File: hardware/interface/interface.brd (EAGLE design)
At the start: 112 x 83 mm, 8 parts

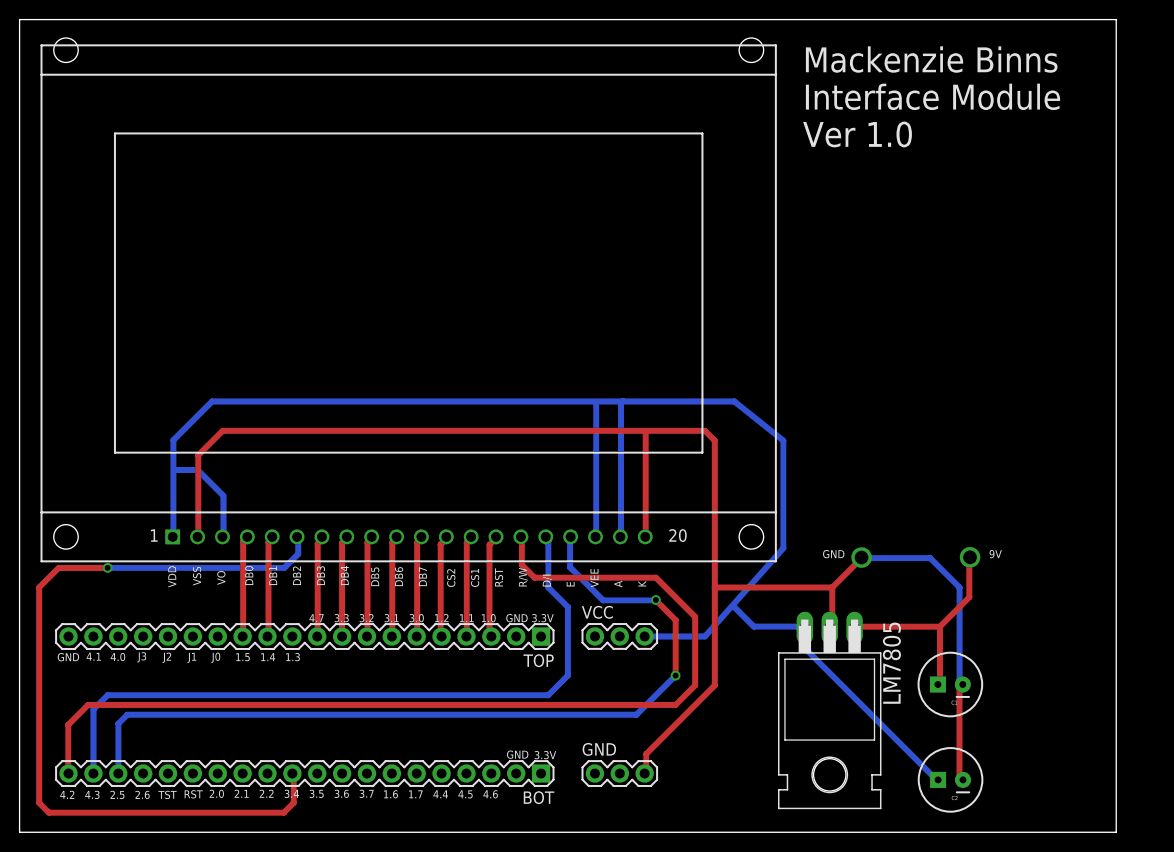
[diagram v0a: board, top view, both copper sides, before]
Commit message: update interface schematic
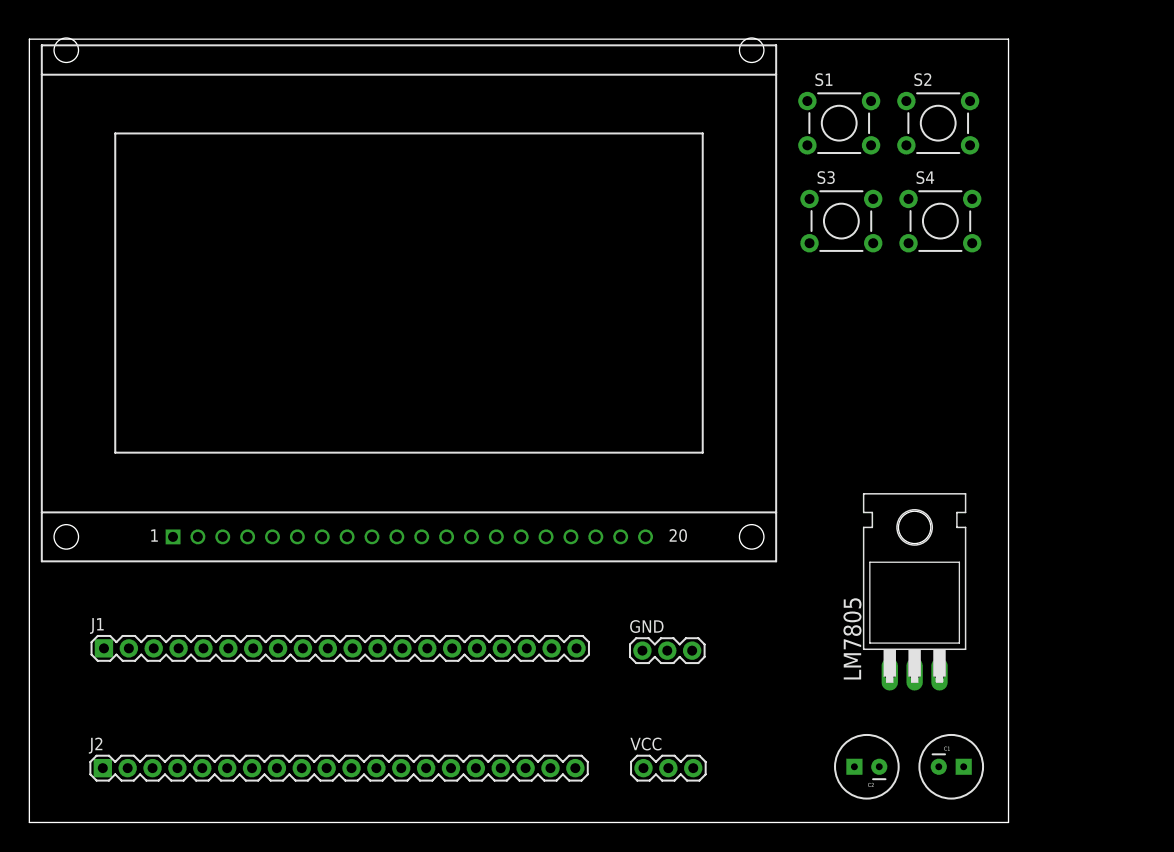
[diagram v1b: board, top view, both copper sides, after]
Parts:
- removed BOT, TOP: (no value), SparkFun-Connectors:1X20
- added J1, J2: (no value), SparkFun-Connectors:1X20
- added S1: Set, SparkFun-Retired:TACTILE-PTH
- added S2: Clear, SparkFun-Retired:TACTILE-PTH
- added S3: Shift Up, SparkFun-Retired:TACTILE-PTH
- added S4: Shift Down, SparkFun-Retired:TACTILE-PTH
- moved LM7805 17.9 mm to (90.4, 25.3), turned to 0 degrees
- moved VCC 14.3 mm to (62.7, 5.55)
- moved GND 13.5 mm to (62.6, 17.6)
- moved C2 8.65 mm to (85.5, 5.69)
- moved C1 8.40 mm to (94.2, 5.69), turned to 0 degrees
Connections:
- new net N$2: S1.1
- new net N$3: S1.3
- new net N$4: S2.1
- new net N$5: S2.3
- new net N$6: S3.1
- new net N$7: S3.3
- new net N$8: S4.1
- new net N$9: S4.3
- net GND: now also GND.1, GND.2, GND.3
- net P1.0: now also J2.18
- net P1.1: now also J2.17
- net P1.2: now also J2.16
- net P1.4: now also J2.9
- net P1.5: now also J2.8
- net P2.5: now also J1.3
- net P3.0: now also J2.15
- net P3.1: now also J2.14
- net P3.2: now also J2.13
- net P3.3: now also J2.12
- net P3.4: now also J1.12
- net P4.2: now also J1.1
- net P4.3: now also J1.2
- net P4.7: now also J2.11
- net VCC: now also VCC.1, VCC.2, VCC.3
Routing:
- net N$29: track 119.7 -> 0.00 mm
- net N$1: track 104.6 -> 0.00 mm
- net N$18: track 99.8 -> 0.00 mm
- net N$9: track 81.4 -> 0.00 mm, vias 1 -> 0
- net N$20: track 72.6 -> 0.00 mm, vias 1 -> 0
- net N$19: track 71.4 -> 0.00 mm
- net N$26: track 29.6 -> 0.00 mm
- net N$27: track 23.2 -> 0.00 mm
- net N$30: track 21.5 -> 0.00 mm
- net N$3: track 14.0 -> 0.00 mm
- net N$4: track 13.9 -> 0.00 mm
- net N$22: track 13.3 -> 0.00 mm
- net N$6: track 10.8 -> 0.00 mm
- net N$17: track 10.5 -> 0.00 mm
- net N$7: track 10.5 -> 0.00 mm
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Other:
- board size 112 x 83 mm -> 100 x 80 mm
- board text added: "Interface Board Derailleurs"
- board text removed: "1.4 1.3"
- board text removed: "1.5"
- board text removed: "1.6 1.7 4.4 4.5 4.6"
- board text removed: "2.0 2.1 2.2 3.4 3.5 3.6 3.7"
- board text removed: "3.3V"
- board text removed: "4.0"
- board text removed: "4.1"
- board text removed: "4.2 4.3 2.5 2.6"
- board text removed: "4.7 3.3 3.2 3.1 3.0 1.2 1.1 1.0 GND 3.3V"
- board text removed: "9V"
- board text removed: "CS2 CS1 RST R/W D/I E VEE A K"
- board text removed: "DB0 DB1 DB2 DB3 DB4"
- board text removed: "DB5 DB6 DB7"
- board text removed: "GND"
- board text removed: "J0"
- board text removed: "J1"
- board text removed: "J2"
- board text removed: "J3"
- board text removed: "Mackenzie Binns Interface Module Ver 1.0"
- board text removed: "RST"
- board text removed: "TST"
- board text removed: "VDD"
- board text removed: "VO"
- board text removed: "VSS"

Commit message: finish boards
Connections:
- removed net N$2: S1.1
- removed net N$3: S1.3
- removed net N$4: S2.1
- removed net N$5: S2.3
- removed net N$6: S3.1
- removed net N$7: S3.3
- removed net N$8: S4.1
- removed net N$9: S4.3
- new net P2.0: J1.7, S1.3
- new net P2.6: J1.4, S2.3
- new net P3.5: J1.11, S3.3
- new net P3.6: J1.12, S4.3
- net GND: now also S1.1, S2.1, S3.1, S4.1
- net P3.4: now also J1.10; no longer J1.12
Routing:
- net GND: track 0.00 -> 179.0 mm
- net VCC: track 0.00 -> 119.6 mm
- net P2.6: track 0.00 -> 98.8 mm
- net P2.0: track 0.00 -> 82.9 mm
- net P4.7: track 0.00 -> 74.6 mm
- net P3.6: track 0.00 -> 74.6 mm
- net P3.5: track 0.00 -> 72.5 mm
- net P3.2: track 0.00 -> 62.7 mm, vias 0 -> 1
- net P3.0: track 0.00 -> 50.8 mm, vias 0 -> 1
- net P4.2: track 0.00 -> 48.9 mm
- net P4.3: track 0.00 -> 47.8 mm
- net P2.5: track 0.00 -> 47.3 mm
- net P3.1: track 0.00 -> 46.8 mm, vias 0 -> 1
- net P1.5: track 0.00 -> 46.2 mm
- net P1.4: track 0.00 -> 40.4 mm, vias 0 -> 1
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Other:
- board text added: "Clear"
- board text added: "Set"
- board text added: "Shift Down"
- board text added: "Shift Up"

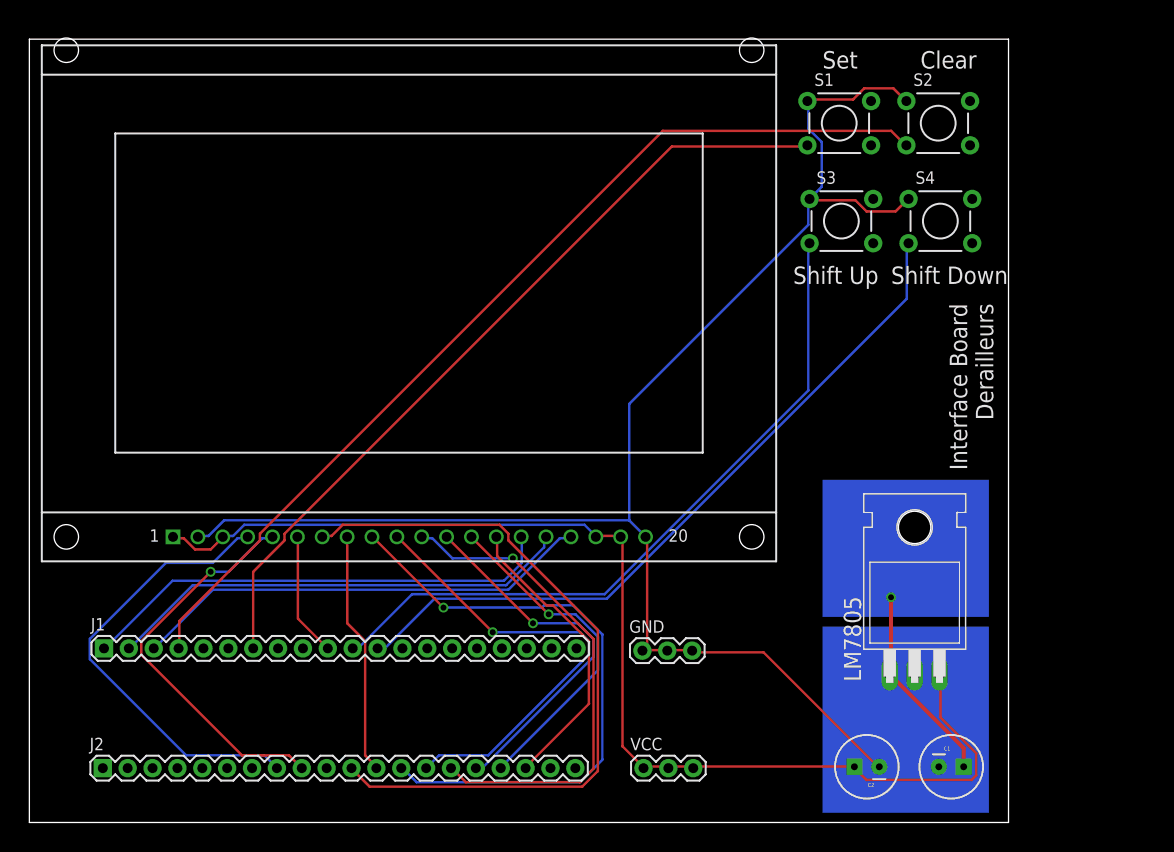
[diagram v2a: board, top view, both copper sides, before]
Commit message: Finish routing all boards, schematics are consitant, and all deliverable requirements are met..
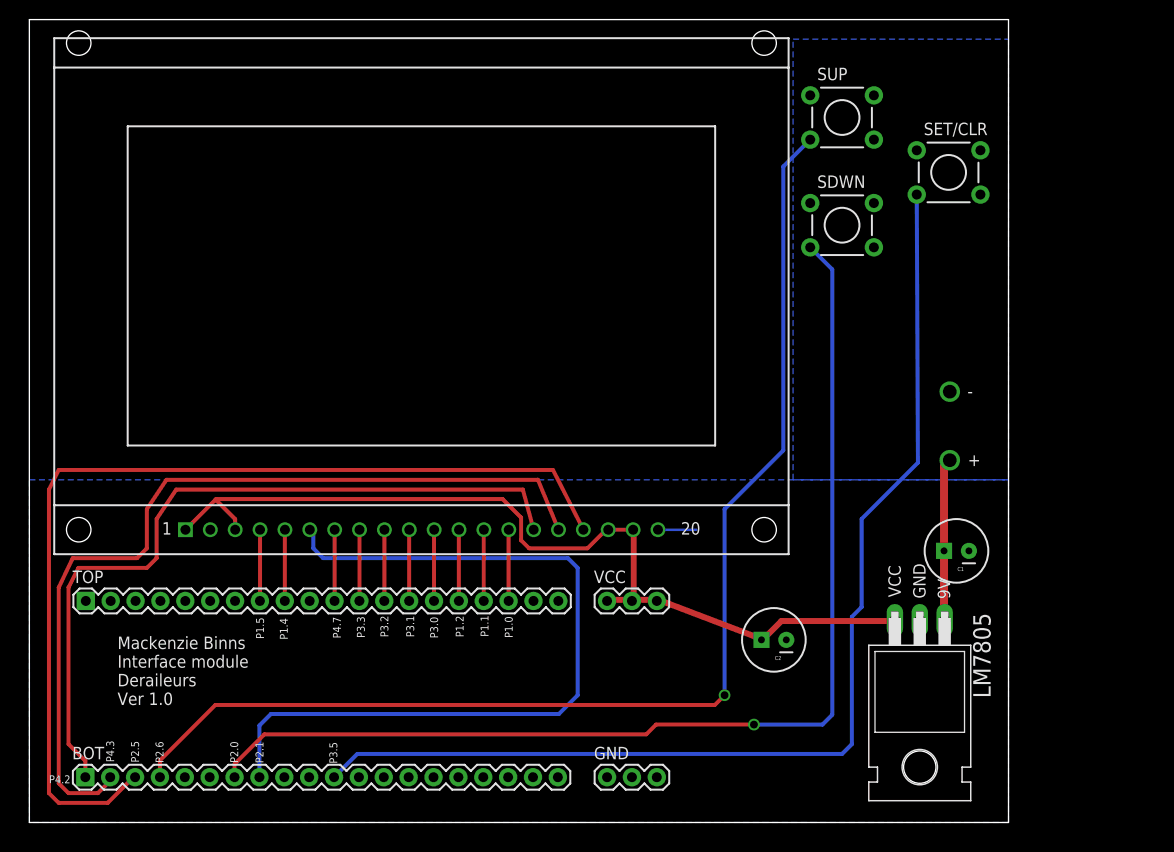
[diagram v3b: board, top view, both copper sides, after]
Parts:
- removed J1, J2: (no value), SparkFun-Connectors:1X20
- removed S1: Set, SparkFun-Retired:TACTILE-PTH
- removed S2: Clear, SparkFun-Retired:TACTILE-PTH
- removed S3: Shift Up, SparkFun-Retired:TACTILE-PTH
- removed S4: Shift Down, SparkFun-Retired:TACTILE-PTH
- added BOT, TOP: 3.3v, SparkFun-Connectors:1X20
- added SDWN, SET/CLR, SUP: SWITCH-MOMENTARY-2PTH, SparkFun-Electromechanical:TACTILE-PTH
- GND: value (none) -> 0v
- VCC: value (none) -> 5v
- moved C1 22.1 mm to (94.7, 27.7), turned to 180 degrees
- moved VCC 17.5 mm to (59.0, 22.6)
- moved C2 16.1 mm to (76.0, 18.6)
- moved LM7805 14.8 mm to (90.9, 10.5), turned to 180 degrees
- moved GND 13.4 mm to (59.0, 4.62)
- moved U$1 1.46 mm to (2.54, 27.4)
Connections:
- removed net P3.4: J1.10, U$1.6
- removed net P3.6: J1.12, S4.3
- new net P2.1: BOT.8, U$1.6
- net GND: now also SDWN.1, SET/CLR.1, SUP.1; no longer S1.1, S2.1, S3.1, S4.1
- net P1.0: now also TOP.18; no longer J2.18
- net P1.1: now also TOP.17; no longer J2.17
- net P1.2: now also TOP.16; no longer J2.16
- net P1.4: now also TOP.9; no longer J2.9
- net P1.5: now also TOP.8; no longer J2.8
- net P2.0: now also BOT.7, SDWN.3; no longer J1.7, S1.3
- net P2.5: now also BOT.3; no longer J1.3
- net P2.6: now also BOT.4, SUP.3; no longer J1.4, S2.3
- net P3.0: now also TOP.15; no longer J2.15
- net P3.1: now also TOP.14; no longer J2.14
- net P3.2: now also TOP.13; no longer J2.13
- net P3.3: now also TOP.12; no longer J2.12
- net P3.5: now also BOT.11, SET/CLR.3; no longer J1.11, S3.3
- net P4.2: now also BOT.1; no longer J1.1
- net P4.3: now also BOT.2; no longer J1.2
- net P4.7: now also TOP.11; no longer J2.11
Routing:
- net GND: track 179.0 -> 4.03 mm, vias 0 -> 1
- net P2.1: track 0.00 -> 81.9 mm
- net P3.6: track 74.6 -> 0.00 mm
- net P4.7: track 74.6 -> 7.48 mm
- net P3.2: track 62.7 -> 7.28 mm, vias 1 -> 0
- net P2.5: track 47.3 -> 100.9 mm
- net P3.0: track 50.8 -> 7.28 mm, vias 1 -> 0
- net P4.3: track 47.8 -> 88.9 mm
- net P3.5: track 72.5 -> 113.2 mm
- net P3.1: track 46.8 -> 7.28 mm, vias 1 -> 0
- net P1.5: track 46.2 -> 7.29 mm
- net P1.4: track 40.4 -> 7.28 mm, vias 1 -> 0
- net P1.2: track 37.9 -> 7.28 mm, vias 1 -> 0
- net P2.0: track 82.9 -> 113.1 mm, vias 0 -> 1
- net P4.2: track 48.9 -> 78.0 mm
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- added copper zone on layer 16, net GND
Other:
- board size 100 x 80 mm -> 100 x 82 mm
- board text added: "+"
- board text added: "-"
- board text added: "9V"
- board text added: "GND"
- board text added: "Mackenzie Binns Interface module Deraileurs Ver 1.0"
- board text added: "P1.0"
- board text added: "P1.1"
- board text added: "P1.2"
- board text added: "P1.4"
- board text added: "P1.5"
- board text added: "P2.0"
- board text added: "P2.1"
- board text added: "P2.5"
- board text added: "P2.6"
- board text added: "P3.0"
- board text added: "P3.1"
- board text added: "P3.2"
- board text added: "P3.3"
- board text added: "P3.5"
- board text added: "P4.2"
- board text added: "P4.3"
- board text added: "P4.7"
- board text added: "VCC"
- board text removed: "Clear"
- board text removed: "Interface Board Derailleurs"
- board text removed: "Set"
- board text removed: "Shift Down"
- board text removed: "Shift Up"
